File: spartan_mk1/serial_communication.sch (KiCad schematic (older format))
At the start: 19 parts

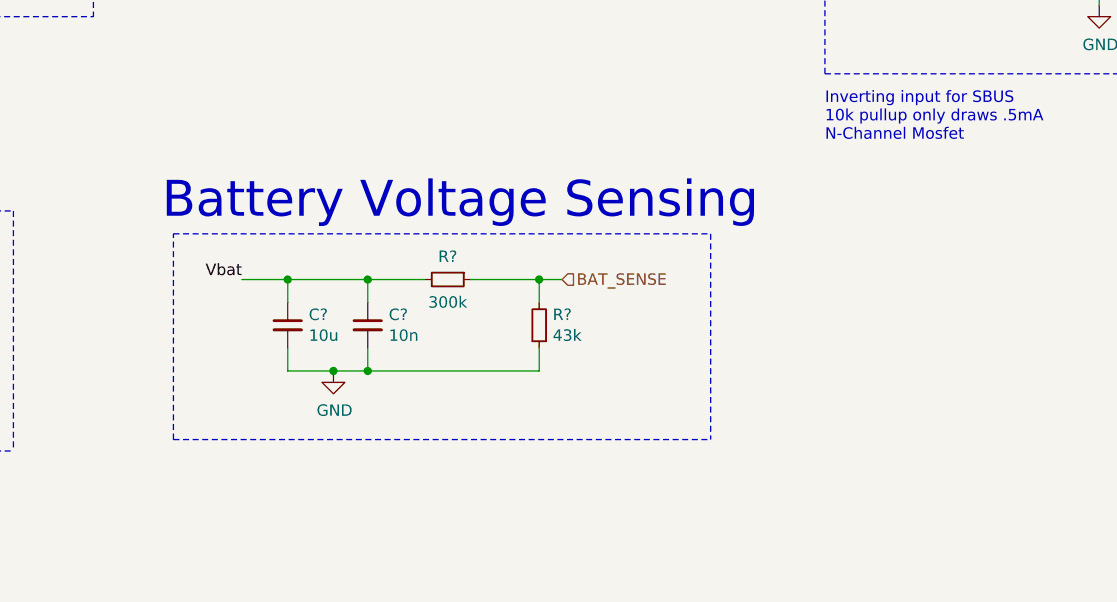
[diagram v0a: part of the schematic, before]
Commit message: Complete schematic with DRC done
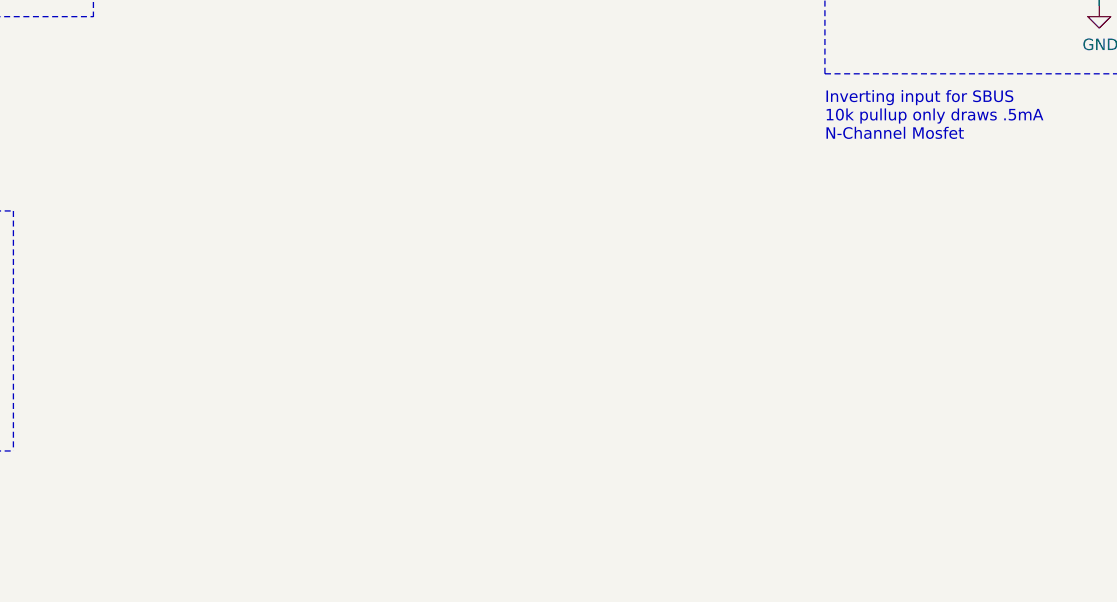
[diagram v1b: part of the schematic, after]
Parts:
- removed C?: 10n, symbol Device:C_Small
- removed C?: 10u, symbol Device:C_Small
- removed R?: 43k, symbol Device:R_Small
- removed R?: 300k, symbol Device:R_Small
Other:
- note removed: "Battery Voltage Sensing"
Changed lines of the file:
@@
 Text Notes 6400 1100 0    157  ~ 0
 USB FB
-Wire Notes Line
-	6000 4300 8350 4300
-Wire Notes Line
-	8350 3400 8350 4300
-Wire Notes Line
-	6000 3400 8350 3400
-Wire Notes Line
-	6000 4300 6000 3400
-Text HLabel 7700 3600 2    50   Input ~ 0
-BAT_SENSE
-Wire Wire Line
-	7600 4000 7600 3900
-Wire Wire Line
-	7700 3600 7600 3600
-Wire Wire Line
-	7600 3600 7300 3600
-Connection ~ 7600 3600
-Wire Wire Line
-	7600 3700 7600 3600
-$Comp
-L Device:R_Small R?
-U 1 1 5FBB08C0
-P 7600 3800
-AR Path="/5F79A745/5FBB08C0" Ref="R?"  Part="1"
-AR Path="/5F78701C/5FBB08C0" Ref="R?"  Part="1"
-F 0 "R?" H 7541 3754 50  0000 R CNN
-F 1 "43k" H 7541 3845 50  0000 R CNN
-F 2 "" H 7600 3800 50  0001 C CNN
-F 3 "~" H 7600 3800 50  0001 C CNN
-	1    7600 3800
-	-1   0    0    1
-$EndComp
-$Comp
-L Device:R_Small R?
-U 1 1 5FBB08C6
-P 7200 3600
-AR Path="/5F79A745/5FBB08C6" Ref="R?"  Part="1"
-AR Path="/5F78701C/5FBB08C6" Ref="R?"  Part="1"
-F 0 "R?" V 7100 3600 50  0000 C CNN
-F 1 "300k" V 7300 3600 50  0000 C CNN
-F 2 "" H 7200 3600 50  0001 C CNN
-F 3 "~" H 7200 3600 50  0001 C CNN
-	1    7200 3600
-	0    1    1    0
-$EndComp
-Wire Wire Line
-	6500 4000 6500 3900
-Wire Wire Line
-	6850 4000 7600 4000
-Connection ~ 6850 4000
-Wire Wire Line
-	6850 4000 6850 3900
-Wire Wire Line
-	6700 4000 6500 4000
-Wire Wire Line
-	6700 4000 6850 4000
-Connection ~ 6700 4000
-$Comp
-L power:GND #PWR?
-U 1 1 5FBB08D3
-P 6700 4000
-AR Path="/5F78701C/5FBB08D3" Ref="#PWR?"  Part="1"
-AR Path="/5F79A745/5FBB08D3" Ref="#PWR?"  Part="1"
-F 0 "#PWR?" H 6700 3750 50  0001 C CNN
-F 1 "GND" H 6705 3827 50  0000 C CNN
-F 2 "" H 6700 4000 50  0001 C CNN
-F 3 "" H 6700 4000 50  0001 C CNN
-	1    6700 4000
-	1    0    0    -1
-$EndComp
-Wire Wire Line
-	7100 3600 6850 3600
-Connection ~ 6850 3600
-Wire Wire Line
-	6850 3600 6850 3700
-Wire Wire Line
-	6300 3600 6500 3600
-Wire Wire Line
-	6500 3600 6850 3600
-Connection ~ 6500 3600
-Wire Wire Line
-	6500 3700 6500 3600
-$Comp
-L Device:C_Small C?
-U 1 1 5FBB08E0
-P 6850 3800
-AR Path="/5F79A745/5FBB08E0" Ref="C?"  Part="1"
-AR Path="/5F78701C/5FBB08E0" Ref="C?"  Part="1"
-F 0 "C?" H 6942 3846 50  0000 L CNN
-F 1 "10n" H 6942 3755 50  0000 L CNN
-F 2 "" H 6850 3800 50  0001 C CNN
-F 3 "~" H 6850 3800 50  0001 C CNN
-	1    6850 3800
-	1    0    0    -1
-$EndComp
-$Comp
-L Device:C_Small C?
-U 1 1 5FBB08E6
-P 6500 3800
-AR Path="/5F79A745/5FBB08E6" Ref="C?"  Part="1"
-AR Path="/5F78701C/5FBB08E6" Ref="C?"  Part="1"
-F 0 "C?" H 6592 3846 50  0000 L CNN
-F 1 "10u" H 6592 3755 50  0000 L CNN
-F 2 "" H 6500 3800 50  0001 C CNN
-F 3 "~" H 6500 3800 50  0001 C CNN
-	1    6500 3800
-	1    0    0    -1
-$EndComp
-Text Label 6300 3600 2    50   ~ 0
-Vbat
-Text Notes 5950 3350 0    157  ~ 0
-Battery Voltage Sensing
 Text Notes 4100 4850 0    157  ~ 0
 GPIO
